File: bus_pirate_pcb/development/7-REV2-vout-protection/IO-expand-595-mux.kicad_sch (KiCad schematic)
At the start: 40 parts, among them Q2 2N7002KT, U10 GS358-FR, U11 GS358-FR, U12 GS358-FR, U13 GS358-FR, U2 AiP74LVC8T245QE24.TR, U4 XL9555QF24, U402 CD4067, U503 74HCT245BQ, U9 GS358-FR

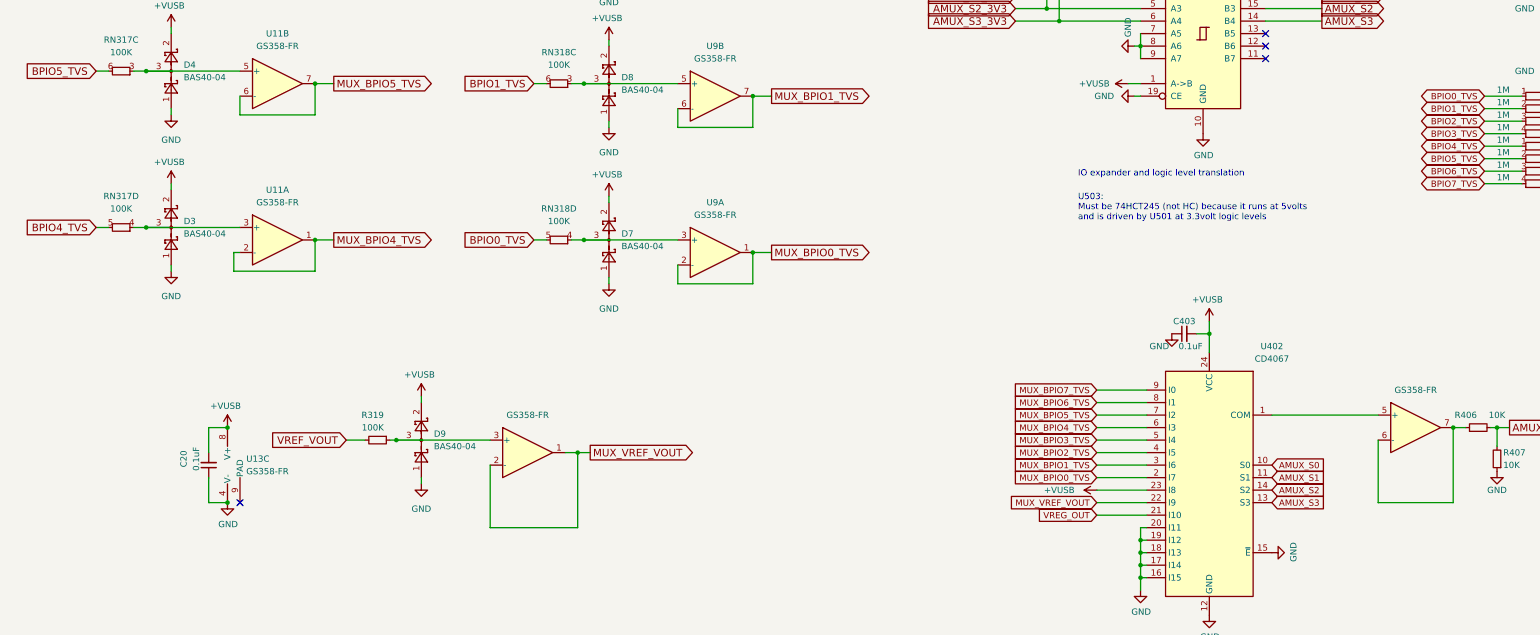
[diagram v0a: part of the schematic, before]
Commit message: 7R2 with vout protection
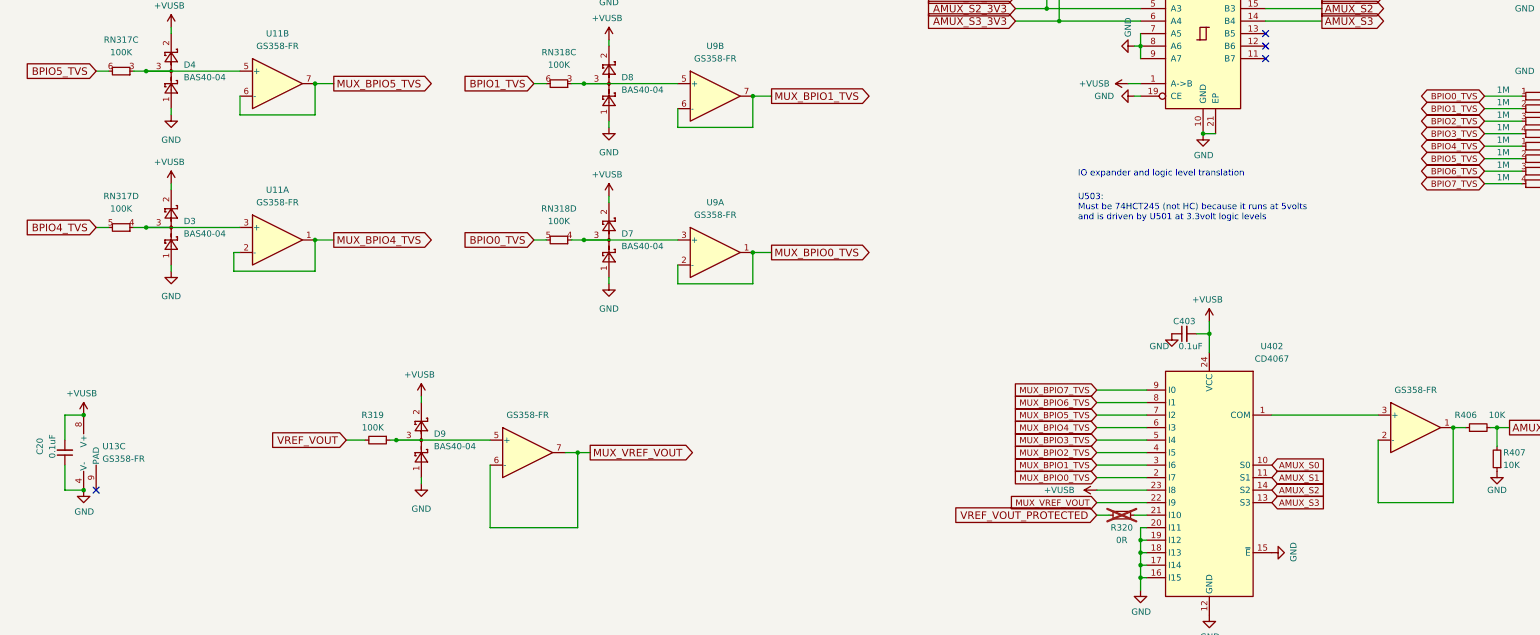
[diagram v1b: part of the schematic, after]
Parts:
- added R320: 0R, Resistor_SMD:R_0402_1005Metric, symbol Device:R_Small
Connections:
- net GND: now also U503.21 (EP)
- net MUX_VREF_VOUT: now also U13.6 (-), U13.7; no longer U13.1, U13.2 (-)
- net at U402.1 (COM): now also U13.3 (+); no longer U13.5 (+)
- net at D9.3, R319.1: now also U13.5 (+); no longer U13.3 (+)
- net VREG_OUT: no longer names the net of U402.21 (I10)
- net VREG_OUT: now also R320.1
- new net: R406.1, U13.1, U13.2 (-)
- new net VREF_VOUT_PROTECTED: R320.2
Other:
- moved on the sheet: C20, U13C
